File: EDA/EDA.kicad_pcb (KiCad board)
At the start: 2 copper layers, 66.5 x 53.8 mm, 30 parts, among them J1 Conn_01x03_Pin, J2 Screw_Terminal_01x02, J3 Conn_01x08_Pin, J4 Conn_01x10_Pin, J5 Conn_01x08_Pin, J6 Conn_01x06_Pin, J7 Screw_Terminal_01x01, M1 Motor_Servo, U1 PMCF8316A1VRGFR, U2 LM2596S-5, U3 LM2596S-5

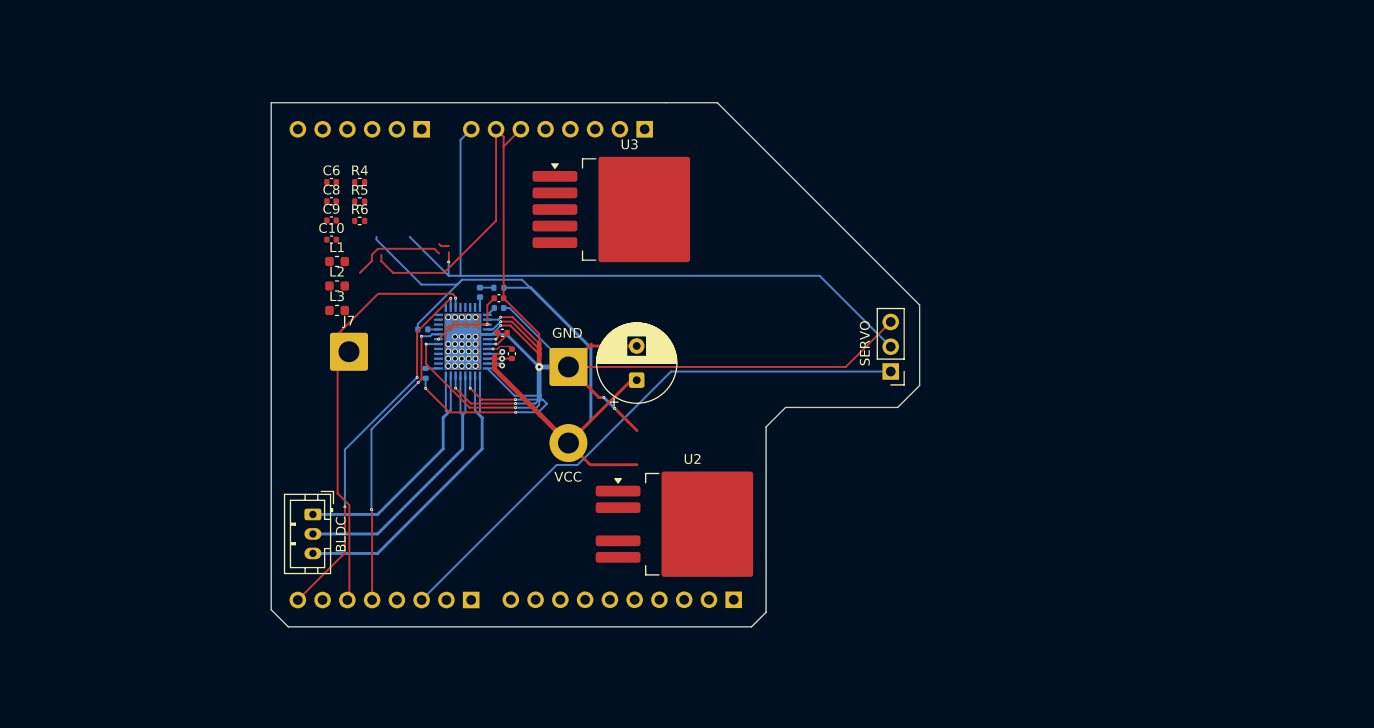
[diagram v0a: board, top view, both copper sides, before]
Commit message: Add No-Connect flags and add labels, create ground terminal for Raspberry Pi.
Started Routing PCB.

- Developed Pi 5V, 5A power supply.
- Working on 5V, 3A servo power supply.
- Yet to begin wiring BLDC motor controller logic.
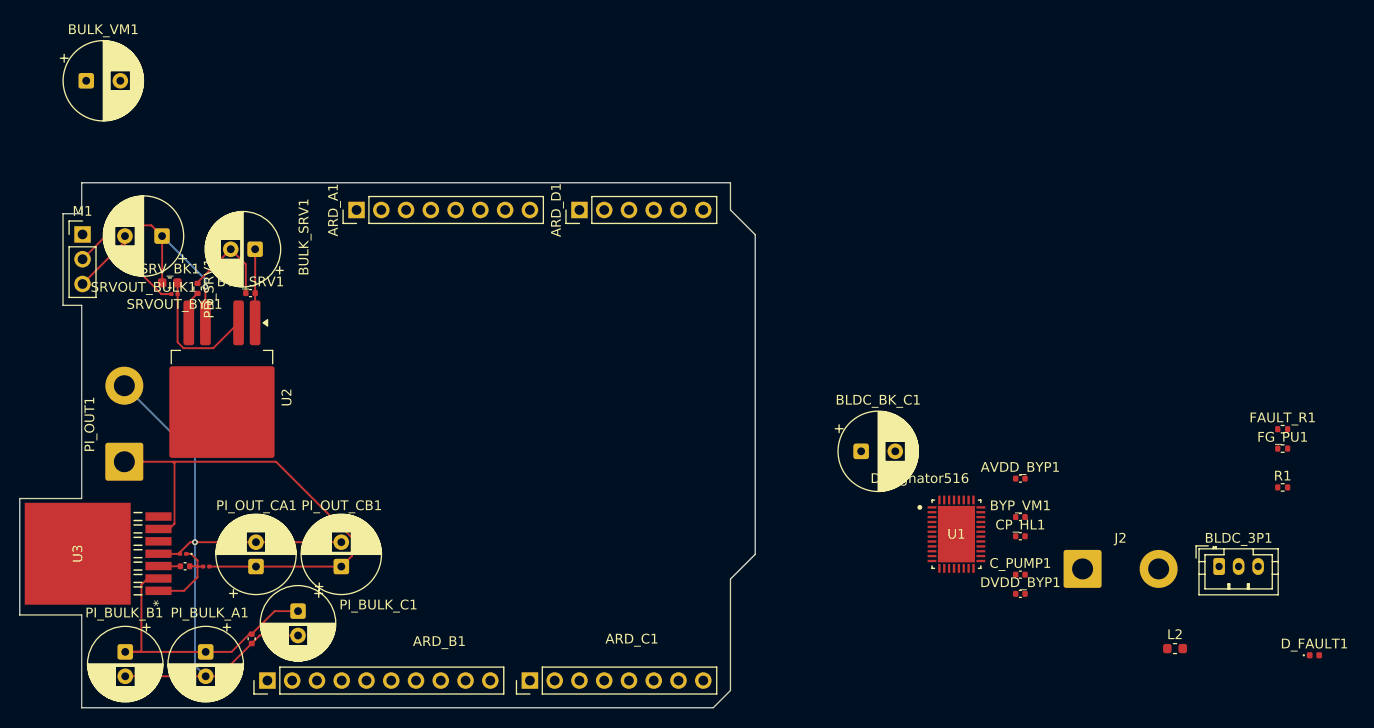
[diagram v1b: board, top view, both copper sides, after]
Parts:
- removed C1: 500uf, Capacitor_THT:CP_Radial_D8.0mm_P3.50mm
- removed C10, C6, C9: 5uf, Capacitor_SMD:C_0402_1005Metric
- removed C2, C3, C5: 1uf, Capacitor_SMD:C_0402_1005Metric
- removed C4: 47nf, Capacitor_SMD:C_0402_1005Metric
- removed C8: 0.1uf, Capacitor_SMD:C_0402_1005Metric
- removed D1: LED, LED_SMD:LED_0402_1005Metric
- removed J1: Conn_01x03_Pin, Connector_JST:JST_PH_B3B-PH-K_1x03_P2.00mm_Vertical
- removed J3, J5: Conn_01x08_Pin, Connector_PinHeader_2.54mm:PinHeader_1x08_P2.54mm_Vertical
- removed J4: Conn_01x10_Pin, Connector_PinHeader_2.54mm:PinHeader_1x10_P2.54mm_Vertical
- removed J6: Conn_01x06_Pin, Connector_PinHeader_2.54mm:PinHeader_1x06_P2.54mm_Vertical
- removed J7: Screw_Terminal_01x01, Connector_Wire:SolderWire-1.5sqmm_1x01_D1.7mm_OD3.9mm
- removed L1, L3: 47uh, Inductor_SMD:L_0603_1608Metric
- removed R2, R3: 5.1k, Resistor_SMD:R_0402_1005Metric
- removed R4: 10k, Resistor_SMD:R_0402_1005Metric
- removed R5, R6: 5k, Resistor_SMD:R_0402_1005Metric
- added ARD_A1: Conn_01x08_Pin, Connector_PinHeader_2.54mm:PinHeader_1x08_P2.54mm_Vertical, F.Cu at (134.0, 73.8)
- added ARD_B1: Conn_01x10_Pin, Connector_PinHeader_2.54mm:PinHeader_1x10_P2.54mm_Vertical, F.Cu at (124.9, 122.0)
- added ARD_C1: Conn_01x08_Pin, Connector_PinHeader_2.54mm:PinHeader_1x08_P2.54mm_Vertical, F.Cu at (151.8, 122.0)
- added ARD_D1: Conn_01x06_Pin, Connector_PinHeader_2.54mm:PinHeader_1x06_P2.54mm_Vertical, F.Cu at (156.9, 73.8)
- added AVDD_BYP1: 1uf, Capacitor_SMD:C_0402_1005Metric, F.Cu at (202.1, 101.3)
- added BLDC_3P1: Conn_01x03_Pin, Connector_JST:JST_PH_B3B-PH-K_1x03_P2.00mm_Vertical, F.Cu at (222.5, 110.3)
- added BLDC_BK_C1: 300uf, Capacitor_THT:CP_Radial_D8.0mm_P3.50mm, F.Cu at (185.8, 98.5)
- added BULK_SRV1: 100uf, Capacitor_THT:CP_Radial_D7.5mm_P2.50mm, F.Cu at (123.6, 77.8)
- added BULK_VM1: 500uf, Capacitor_THT:CP_Radial_D8.0mm_P3.50mm, F.Cu at (106.3, 60.5)
- added BYP_SRV1: 1uf, Capacitor_SMD:C_0402_1005Metric, F.Cu at (123.1, 82.3)
- added BYP_VM1: 1uf, Capacitor_SMD:C_0402_1005Metric, F.Cu at (202.1, 105.2)
- added CP_HL1: 47nf, Capacitor_SMD:C_0402_1005Metric, F.Cu at (202.1, 107.2)
- added C_BOOST1: 0.01uf, Capacitor_SMD:C_0402_1005Metric, F.Cu at (116.4, 110.3)
- added C_PUMP1: 1uf, Capacitor_SMD:C_0402_1005Metric, F.Cu at (202.1, 111.2)
- added DVDD_BYP1: 1uf, Capacitor_SMD:C_0402_1005Metric, F.Cu at (202.1, 113.1)
- added D_FAULT1: LED, LED_SMD:LED_0402_1005Metric, F.Cu at (232.2, 119.4)
- added FAULT_R1: 5.1k, Resistor_SMD:R_0402_1005Metric, F.Cu at (229.0, 96.2)
- added FG_PU1: 5.1k, Resistor_SMD:R_0402_1005Metric, F.Cu at (229.0, 98.2)
- added PD_SRV1: 5k, Resistor_SMD:R_0402_1005Metric, F.Cu at (117.7, 81.8)
- added PI_BK1: 22uh, Inductor_SMD:L_0201_0603Metric, F.Cu at (118.6, 110.3)
- added PI_BULK_A1: 15uf, Capacitor_THT:CP_Radial_D7.5mm_P2.50mm, F.Cu at (118.5, 119.1)
- added PI_BULK_B1: 15uf, Capacitor_THT:CP_Radial_D7.5mm_P2.50mm, F.Cu at (110.3, 119.1)
- added PI_BULK_C1: 15uf, Capacitor_THT:CP_Radial_D7.5mm_P2.50mm, F.Cu at (128.0, 114.9)
- added PI_BYP1: 0.47uf, Capacitor_SMD:C_0402_1005Metric, F.Cu at (123.2, 117.7)
- added PI_CATCH1: D_Schottky, Diode_SMD:D_0201_0603Metric, F.Cu at (116.2, 109.0)
- added PI_OUT1: Screw_Terminal_01x02, Connector_Wire:SolderWire-1.5sqmm_1x02_P7.8mm_D1.7mm_OD3.9mm, F.Cu at (110.2, 99.6)
- added PI_OUT_CA1: 180uf, Capacitor_THT:CP_Radial_D8.0mm_P2.50mm, F.Cu at (123.7, 110.3)
- added PI_OUT_CB1: 180uf, Capacitor_THT:CP_Radial_D8.0mm_P2.50mm, F.Cu at (132.4, 110.3)
- added SRVOUT_BULK1: 470uf, Capacitor_THT:CP_Radial_D8.0mm_P3.80mm, F.Cu at (114.1, 76.4)
- added SRVOUT_BYP1: 1uf, Capacitor_SMD:C_0201_0603Metric, F.Cu at (115.3, 82.4)
- added SRV_BK1: 47uh, Inductor_SMD:L_0603_1608Metric, F.Cu at (114.8, 81.2)
- J2, R1, U1: moved to F.Cu
- U3: value LM2596S-5 -> LM2678S-5; footprint Package_TO_SOT_SMD:TO-263-5_TabPin3 -> LM2678S:TS7B
- moved L2 93.6 mm to (217.9, 118.7)
- moved R1 88.7 mm to (229.0, 102.2), turned to 0 degrees
- moved M1 84.1 mm to (105.9, 76.3), turned to 0 degrees
- moved U3 66.7 mm to (105.4, 109.0), turned to 90 degrees
- moved J2 56.6 mm to (208.5, 110.6), turned to 0 degrees
- moved U1 54.3 mm to (195.5, 107.0), turned to 0 degrees
- moved U2 50.0 mm to (120.2, 93.0), turned to -90 degrees
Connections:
- M1 pad 1: Net-(J3-Pin_3) -> SRV_PWM
- M1 pad 2: Net-(M1-+) -> +5V
- U2 pad 4: Net-(M1-+) -> +5V
- U3 pad 1: +7.5V -> Net-(PI_CATCH1-K)
- U3 pad 2: Net-(U3-OUT) -> +7.5V
- U3 pad 3: GND -> Net-(U3-BOOST)
- U3 pad 4: Net-(J7-Pin_1) -> GND
- U3 pad 5: Net-(U3-~{ON}/OFF) -> unconnected-(U3-NC-Pad5)
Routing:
- net GND: track 213.7 -> 97.4 mm, vias 43 -> 1
- net (no net): track 82.7 -> 0.00 mm, vias 1 -> 0
- net +5V: track 0.00 -> 78.5 mm, vias 0 -> 1
- net Net-(J3-Pin_3): track 57.8 -> 0.00 mm
- net +7.5V: track 87.3 -> 37.6 mm, vias 3 -> 0
- net Net-(ARD_C1-Pin_6): track 42.9 -> 0.00 mm, vias 1 -> 0
- net Net-(ARD_C1-Pin_8): track 38.4 -> 0.00 mm, vias 3 -> 0
- net Net-(BLDC_3P1-Pin_3): track 34.1 -> 0.00 mm
- net Net-(BLDC_3P1-Pin_2): track 31.3 -> 0.00 mm
- net Net-(ARD_C1-Pin_5): track 31.0 -> 0.00 mm, vias 3 -> 0
- net Net-(BLDC_3P1-Pin_1): track 28.4 -> 0.00 mm
- net Net-(U2-OUT): track 0.00 -> 13.7 mm
- net Net-(PI_CATCH1-K): track 0.00 -> 9.12 mm
- net Net-(U1-AVDD): track 8.62 -> 0.00 mm, vias 2 -> 0
- net Net-(U2-~{ON}/OFF): track 0.00 -> 3.40 mm
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- removed copper zone on F.Cu, net (none)
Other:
- board size 66.5 x 53.8 mm -> 75.4 x 53.8 mm
- board text removed: "BLDC"
- board text removed: "GND"
- board text removed: "SERVO"
- board text removed: "VCC"

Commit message: Add initial EDA project files and configuration
- Created EDA.step file for project steps.
- Added autosave configuration for EDA.kicad_prl with board settings, visibility options, and net inspector panel configurations.
- Introduced lock files for PCB and schematic with hostname and username information.

Add components table to README

Added a table listing various components with their products and prices.

Add new symbols and footprints for UCY2D181MHD3TN and VS-6TQ045S-M3 components

- Created symbol for UCY2D181MHD3TN with properties including reference, value, footprint, and datasheet.
- Added footprint for UCY2D181MHD3TN with dimensions and pad specifications.
- Created symbol for VS-6TQ045S-M3 with properties including reference, value, footprint, and datasheet link.
- Added multiple footprints for VS-6TQ045S-M3, including DPAK_045S-M3_VIS, DPAK_045S-M3_VIS-L, and DPAK_045S-M3_VIS-M with detailed specifications.
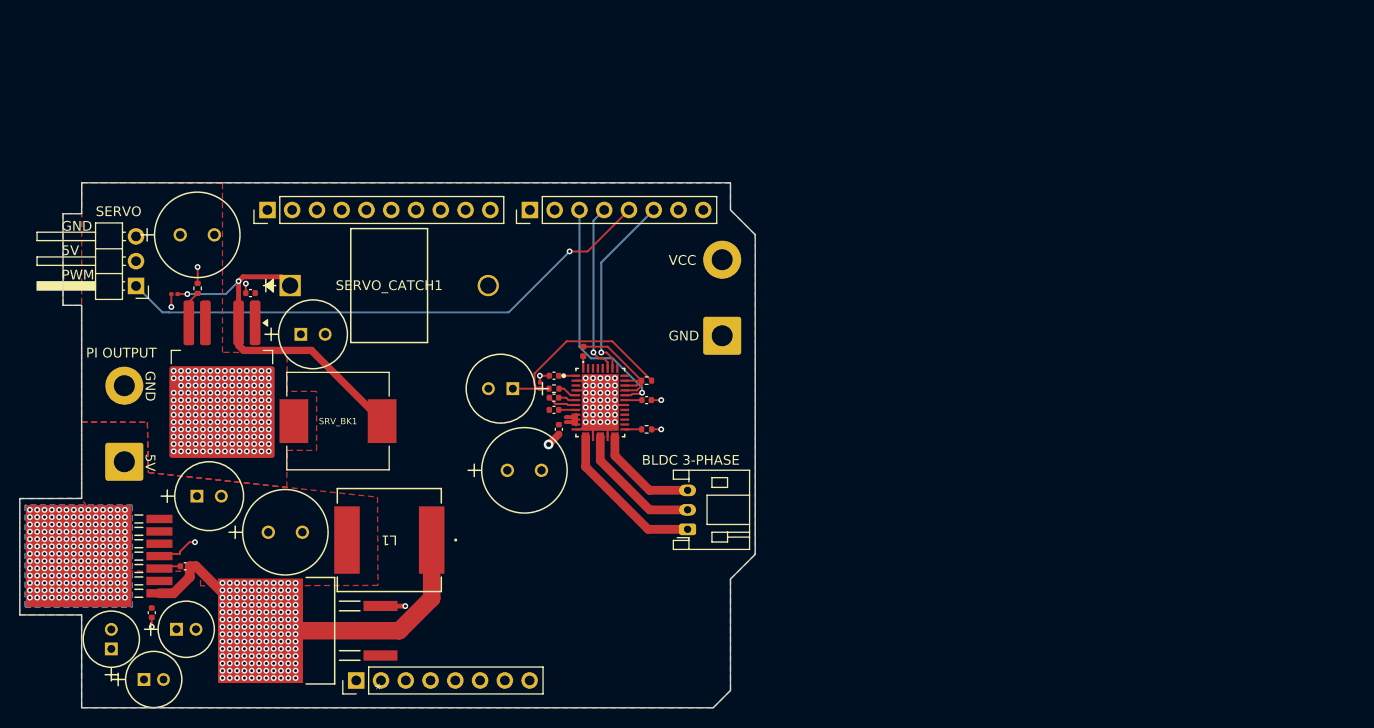
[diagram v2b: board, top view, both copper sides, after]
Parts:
- removed ARD_D1: Conn_01x06_Pin, Connector_PinHeader_2.54mm:PinHeader_1x06_P2.54mm_Vertical
- removed BLDC_BK_C1: 300uf, Capacitor_THT:CP_Radial_D8.0mm_P3.50mm
- removed BULK_SRV1: 100uf, Capacitor_THT:CP_Radial_D7.5mm_P2.50mm
- removed BULK_VM1: 500uf, Capacitor_THT:CP_Radial_D8.0mm_P3.50mm
- removed FAULT_R1: 5.1k, Resistor_SMD:R_0402_1005Metric
- removed L2: 47uh, Inductor_SMD:L_0603_1608Metric
- removed PI_BK1: 22uh, Inductor_SMD:L_0201_0603Metric
- removed PI_BULK_A1, PI_BULK_B1, PI_BULK_C1: 15uf, Capacitor_THT:CP_Radial_D7.5mm_P2.50mm
- removed PI_OUT_CA1, PI_OUT_CB1: 180uf, Capacitor_THT:CP_Radial_D8.0mm_P2.50mm
- added BK_BULK1: 100uf, 860040573004:CAP_WCAP-ATUL_06.3X11.0_WRE, F.Cu at (150.0, 92.1)
- added BK_BYP1: 1uf, Capacitor_SMD:C_0201_0603Metric, F.Cu at (152.8, 91.8)
- added BULK_VM2: 470uf, 16ZLH470MEFCT78X11.5:CAP_YX_8X11P5_RUB, F.Cu at (149.5, 100.5)
- added L1: SRP1038WA-220M, SRP1038WA-220M:IND_SRP1038WA-220M_BRN, F.Cu at (137.4, 107.6)
- added PI_BULK1: 15uf, 860160572002:CAP_5X11_WRE, F.Cu at (112.2, 121.9)
- added PI_BULK2: 15uf, 860160572002:CAP_5X11_WRE, F.Cu at (115.5, 116.8)
- added PI_BULK3: 15uf, 860160572002:CAP_5X11_WRE, F.Cu at (108.8, 118.8)
- added PI_OUT2: 470uf, 16ZLH470MEFCT78X11.5:CAP_YX_8X11P5_RUB, F.Cu at (124.9, 106.8)
- added PI_OUT3: 100uf, 860040573004:CAP_WCAP-ATUL_06.3X11.0_WRE, F.Cu at (117.6, 103.1)
- added R_BK1: 5.1k, Resistor_SMD:R_0402_1005Metric, F.Cu at (154.2, 92.1)
- added SERVO_CATCH1: 1N5825, 1N5825:1N5825_MCH, F.Cu at (127.2, 81.5)
- added SRV_BULK1: 100uf, 860040573004:CAP_WCAP-ATUL_06.3X11.0_WRE, F.Cu at (128.3, 86.5)
- BLDC_3P1: footprint Connector_JST:JST_PH_B3B-PH-K_1x03_P2.00mm_Vertical -> Connector_JST:JST_PH_S3B-PH-K_1x03_P2.00mm_Horizontal
- M1: footprint Connector_PinHeader_2.54mm:PinHeader_1x03_P2.54mm_Vertical -> Connector_PinHeader_2.54mm:PinHeader_1x03_P2.54mm_Horizontal
- PI_CATCH1: value D_Schottky -> Schotty Diode; footprint Diode_SMD:D_0201_0603Metric -> VS-6TQ045S-M3:DPAK_045S-M3_VIS
- SRVOUT_BULK1: footprint Capacitor_THT:CP_Radial_D8.0mm_P3.80mm -> 16ZLH470MEFCT78X11.5:CAP_YX_8X11P5_RUB
- SRV_BK1: value 47uh -> 68uh; footprint Inductor_SMD:L_0603_1608Metric -> SPM10065VT-680M-D:IND_SPM10065VT-680M-D
- moved D_FAULT1 81.2 mm to (157.2, 88.2), turned to 90 degrees
- moved FG_PU1 65.6 mm to (163.7, 91.2), turned to 180 degrees
- moved R1 65.5 mm to (163.7, 96.2), turned to 180 degrees
- moved BLDC_3P1 54.6 mm to (167.9, 106.5), turned to 90 degrees
- moved DVDD_BYP1 52.8 mm to (154.2, 90.8), turned to 180 degrees
- moved C_PUMP1 50.7 mm to (154.2, 94.2)
- moved CP_HL1 49.9 mm to (154.2, 93.0)
- moved ARD_B1 48.3 mm to (124.9, 73.8)
- moved ARD_C1 48.3 mm to (151.8, 73.8)
- moved ARD_A1 48.3 mm to (134.0, 122.0)
- moved BYP_VM1 48.2 mm to (154.7, 96.2), turned to 90 degrees
- moved J2 44.0 mm to (171.5, 86.7), turned to 90 degrees
- moved AVDD_BYP1 39.2 mm to (163.7, 93.2), turned to 180 degrees
- moved U1 38.9 mm to (159.0, 93.5)
- moved SRV_BK1 22.3 mm to (132.1, 95.4), turned to 180 degrees
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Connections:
- ARD_C1 pad 3: SRV_PWM -> Net-(ARD_C1-Pin_3)
- ARD_C1 pad 4: unconnected-(ARD_C1-Pin_4-Pad4) -> Net-(ARD_C1-Pin_4)
- ARD_C1 pad 5: Net-(ARD_C1-Pin_5) -> SRV_PWM
- ARD_C1 pad 8: Net-(ARD_C1-Pin_8) -> unconnected-(ARD_C1-Pin_8-Pad8)
- C_BOOST1 pad 2: Net-(PI_CATCH1-K) -> Net-(U3-SW)
- FG_PU1 pad 1: +7.5V -> +3V3
- FG_PU1 pad 2: Net-(U1-FG) -> Net-(D_FAULT1-A)
- M1 pad 2: +5V -> SRV 5V, 3A
- PI_CATCH1 pad 1: Net-(PI_CATCH1-K) -> unconnected-(PI_CATCH1-N/C-Pad1)
- PI_CATCH1 pad 2: GND -> Net-(U3-SW)
- PI_OUT1 pad 1: +5V -> PI 5V, 5A
- SRVOUT_BULK1 pad 1: +5V -> SRV 5V, 3A
- SRV_BK1 pad 1: +5V -> Net-(U2-OUT)
- SRV_BK1 pad 2: Net-(U2-OUT) -> SRV 5V, 3A
- U1 pad 13: Net-(BLDC_3P1-Pin_3) -> Net-(BLDC_3P1-Pin_1)
- U1 pad 14: Net-(BLDC_3P1-Pin_3) -> Net-(BLDC_3P1-Pin_1)
- U1 pad 19: Net-(BLDC_3P1-Pin_1) -> Net-(BLDC_3P1-Pin_3)
- U1 pad 20: Net-(BLDC_3P1-Pin_1) -> Net-(BLDC_3P1-Pin_3)
- U1 pad 28: Net-(ARD_C1-Pin_5) -> Net-(ARD_C1-Pin_3)
- U1 pad 29: Net-(U1-FG) -> Net-(D_FAULT1-A)
- U1 pad 3: Net-(U1-FB_BK) -> unconnected-(U1-FB_BK-Pad3)
- U1 pad 30: Net-(U1-FG) -> Net-(D_FAULT1-A)
- U1 pad 31: Net-(U1-FG) -> Net-(D_FAULT1-A)
- U1 pad 34: Net-(ARD_C1-Pin_8) -> Net-(ARD_C1-Pin_6)
- U1 pad 35: Net-(ARD_C1-Pin_6) -> Net-(ARD_C1-Pin_4)
- U2 pad 4: +5V -> SRV 5V, 3A
- U3 pad 1: Net-(PI_CATCH1-K) -> Net-(U3-SW)
- U3 pad 6: +5V -> PI 5V, 5A
- U3 pad 8: (no net) -> GND
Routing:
- net +5V: track 78.5 -> 0.00 mm, vias 1 -> 0
- net GND: track 97.4 -> 26.3 mm, vias 1 -> 394
- net SRV_PWM: track 0.00 -> 56.0 mm, vias 0 -> 1
- net Net-(U3-SW): track 0.00 -> 39.8 mm, vias 0 -> 154
- net +7.5V: track 37.6 -> 3.10 mm
- net Net-(ARD_C1-Pin_3): track 0.00 -> 24.6 mm, vias 0 -> 1
- net Net-(U2-OUT): track 13.7 -> 37.2 mm, vias 0 -> 2
- net +3V3: track 0.00 -> 20.7 mm
- net Net-(ARD_C1-Pin_6): track 0.00 -> 19.3 mm, vias 0 -> 1
- net Net-(ARD_C1-Pin_4): track 0.00 -> 17.6 mm, vias 0 -> 1
- net Net-(BLDC_3P1-Pin_1): track 0.00 -> 16.7 mm
- net Net-(BLDC_3P1-Pin_2): track 0.00 -> 14.0 mm
- net Net-(D_FAULT1-A): track 0.00 -> 13.6 mm
- net Net-(BLDC_3P1-Pin_3): track 0.00 -> 11.4 mm
- net Net-(PI_CATCH1-K): track 9.12 -> 0.00 mm
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- added copper zone on F.Cu, net +7.5V
- added copper zone on B.Cu, net GND
- added copper zone on F.Cu, net PI 5V, 5A
- added copper zone on F.Cu, net SRV 5V, 3A
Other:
- outline, holes or cut-outs redrawn
- board text added: "5V"
- board text added: "BLDC 3-PHASE"
- board text added: "GND"
- board text added: "PI OUTPUT"
- board text added: "PWM"
- board text added: "SERVO"
- board text added: "VCC"

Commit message: Started Routing PCB.
- Developed Pi 5V, 5A power supply.
- Working on 5V, 3A servo power supply.
- Yet to begin wiring BLDC motor controller logic.
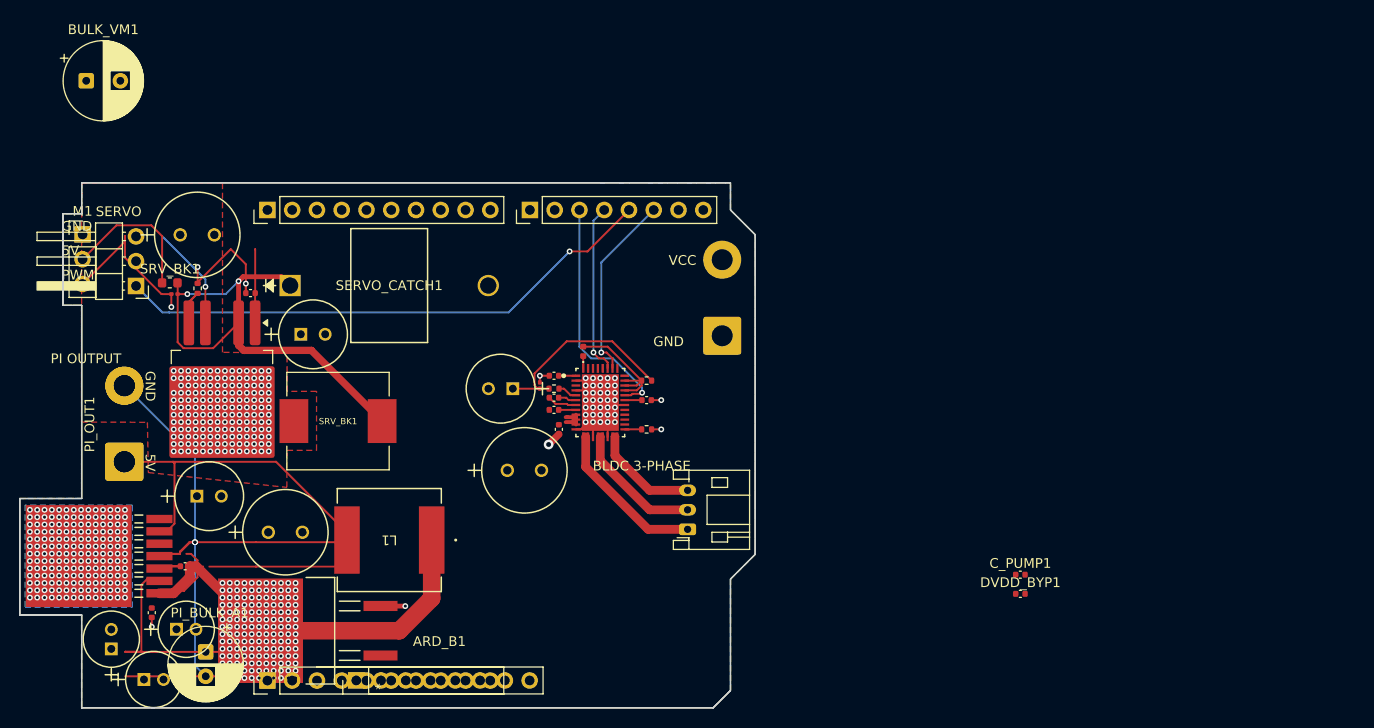
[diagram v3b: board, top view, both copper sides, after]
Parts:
- added ARD_B1: Conn_01x10_Pin, Connector_PinHeader_2.54mm:PinHeader_1x10_P2.54mm_Vertical, F.Cu at (124.9, 122.0)
- added BULK_VM1: 500uf, Capacitor_THT:CP_Radial_D8.0mm_P3.50mm, F.Cu at (106.3, 60.5)
- added C_PUMP1: 1uf, Capacitor_SMD:C_0402_1005Metric, F.Cu at (202.1, 111.2)
- added DVDD_BYP1: 1uf, Capacitor_SMD:C_0402_1005Metric, F.Cu at (202.1, 113.1)
- added M1: Motor_Servo, Connector_PinHeader_2.54mm:PinHeader_1x03_P2.54mm_Vertical, F.Cu at (105.9, 76.3)
- added PI_BULK_A1: 15uf, Capacitor_THT:CP_Radial_D7.5mm_P2.50mm, F.Cu at (118.5, 119.1)
- added PI_OUT1: Screw_Terminal_01x02, Connector_Wire:SolderWire-1.5sqmm_1x02_P7.8mm_D1.7mm_OD3.9mm, F.Cu at (110.2, 99.6)
- added SRV_BK1: 47uh, Inductor_SMD:L_0603_1608Metric, F.Cu at (114.8, 81.2)
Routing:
- net GND: track 26.3 -> 123.7 mm, vias 394 -> 395
- net 60: track 0.00 -> 78.5 mm, vias 0 -> 1
- net +7.5V: track 3.10 -> 40.7 mm
- net unconnected-(ARD_B1-Pin_9-Pad9): track 0.00 -> 13.7 mm
- net +3V3: track 20.7 -> 29.8 mm
- net 61: track 0.00 -> 3.40 mm
- net unconnected-(U1-FB_BK-Pad3): track 0.00 -> 2.26 mm
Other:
- outline, holes or cut-outs redrawn
